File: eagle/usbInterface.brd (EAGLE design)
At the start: 40 x 20 mm, 22 parts

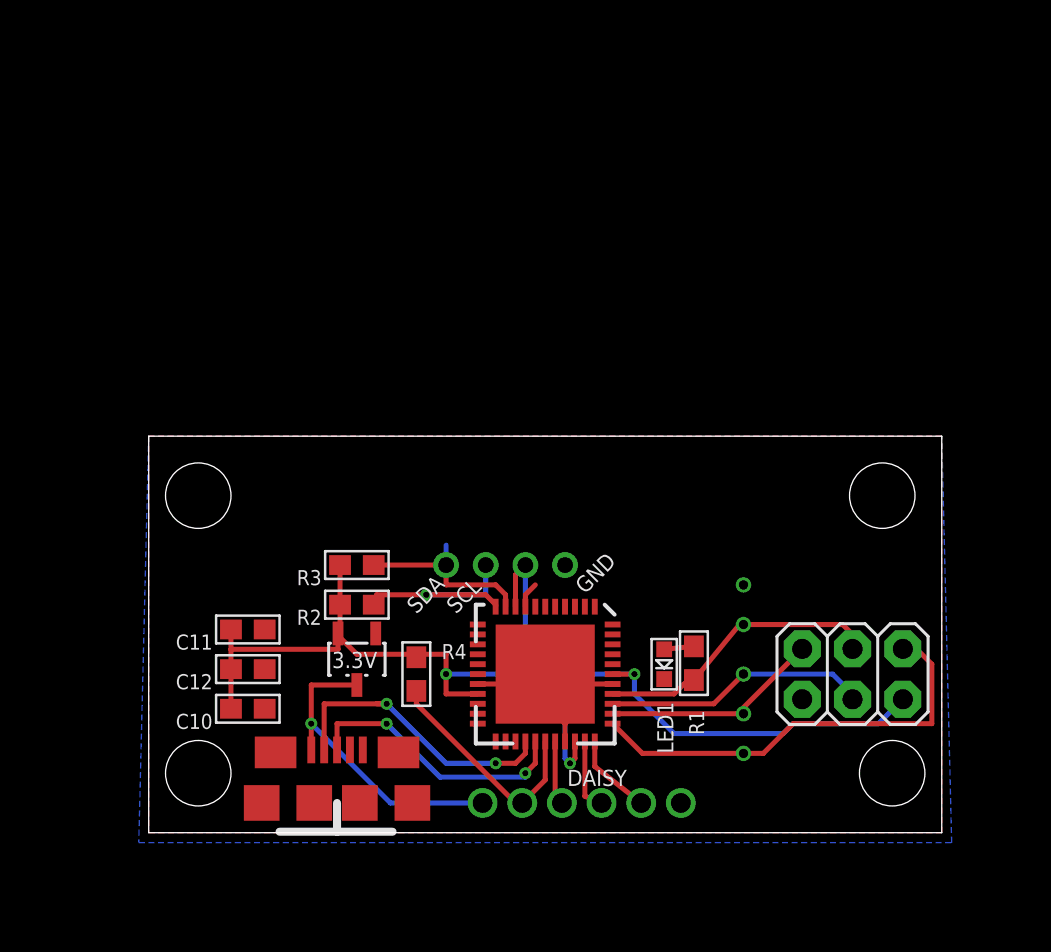
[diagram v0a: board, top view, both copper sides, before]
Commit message: large amount of work on 1x4 ewod array
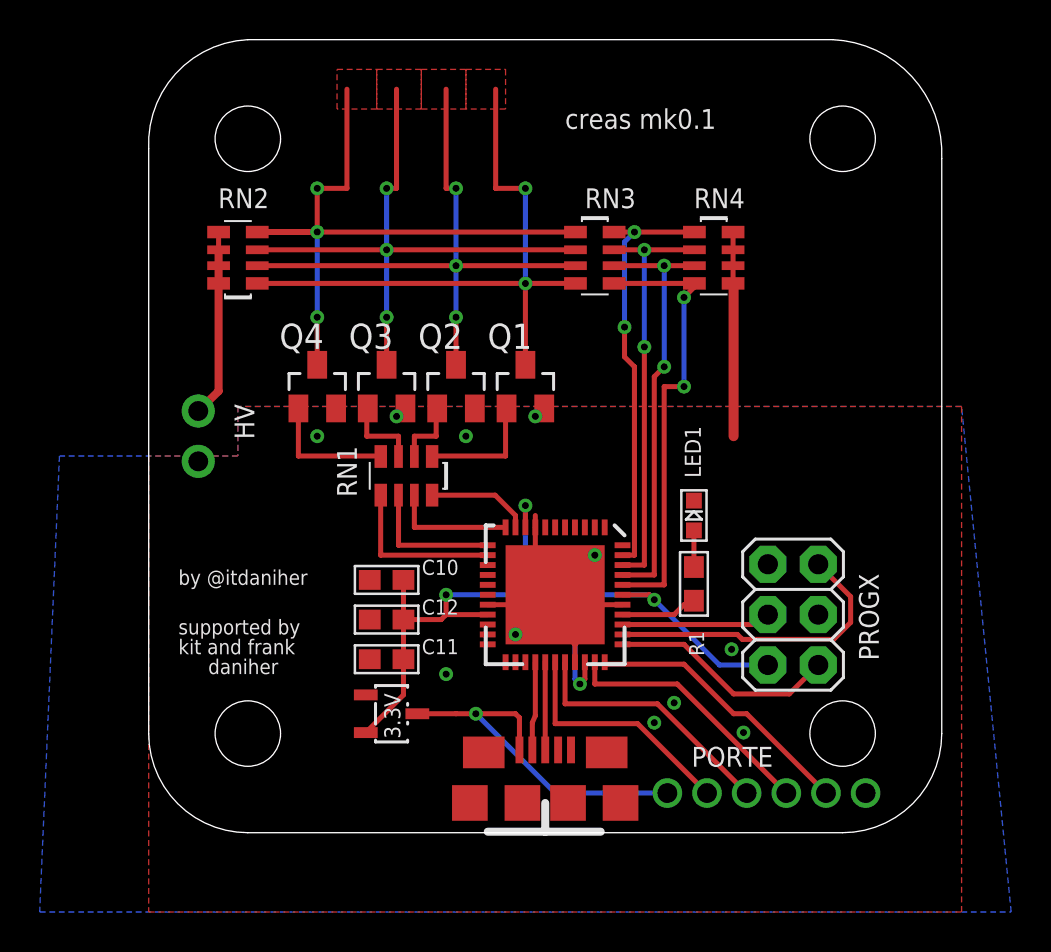
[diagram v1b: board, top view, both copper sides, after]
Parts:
- removed DAISY: (no value), nonolith:1X06_ROUND_2MM
- removed JP1, JP2, SCL, SDA: (no value), nonolith:1X01_2MM
- removed R2, R3: 4.7K, nonolith:0603
- removed R4: 4.7k, nonolith:0603
- added HV: (no value), nonolith:1X02_ROUND
- added PORTE: (no value), nonolith:1X06_ROUND_2MM
- added Q1, Q2, Q3, Q4: (no value), dp_devices:SOT23
- added RN1, RN2, RN3, RN4: (no value), nonolith:RN8P-4R-CRA06S
- moved U$3 18.2 mm to (-15.0, 35.0)
- moved U$4 18.1 mm to (15.0, 35.0)
- moved CN1 10.5 mm to (0.00, 1.50)
- moved C10 9.55 mm to (-8.00, 12.8), turned to 0 degrees
- moved LED1 7.65 mm to (7.50, 16.0), turned to 0 degrees
- moved C12 7.43 mm to (-8.00, 10.8), turned to 0 degrees
- moved C11 7.16 mm to (-8.00, 8.75), turned to 0 degrees
- moved PROGX 4.24 mm to (12.5, 11.0), turned to 90 degrees
- moved U$5 4.03 mm to (2.40, 10.1)
- moved XM1 4.03 mm to (0.50, 12.0)
- moved R1 4.00 mm to (7.50, 12.6)
- moved 3.3V 3.26 mm to (-7.75, 6.00), turned to 90 degrees
- moved U$1 3.20 mm to (-15.0, 5.00)
- moved U$2 3.20 mm to (15.0, 5.00)
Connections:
- removed net SCL: R2.1, SCL.1, XM1.11
- removed net SDA: R3.1, SDA.1, XM1.10
- new net ADCA: RN3.5, RN4.4, XM1.40
- new net ADCB: RN3.6, RN4.3, XM1.41
- new net ADCC: RN3.7, RN4.2, XM1.42
- new net ADCD: RN3.8, RN4.1, XM1.43
- new net CELLA: Q1.3, RN2.1, RN3.4
- new net CELLB: Q2.3, RN2.2, RN3.3
- new net CELLC: Q3.3, RN2.3, RN3.2
- new net CELLD: Q4.3, RN2.4, RN3.1
- new net GATEA: Q1.1, RN1.1
- new net GATEB: Q2.1, RN1.2
- new net GATEC: Q3.1, RN1.3
- new net GATED: Q4.1, RN1.4
- new net HV: HV.1, RN2.5, RN2.6, RN2.7, RN2.8
- new net OC0A: RN1.8, XM1.10
- new net OC0B: RN1.7, XM1.11
- new net OC0C: RN1.6, XM1.12
- new net OC0D: RN1.5, XM1.13
- net 3.3V: no longer JP2.1, R2.2, R3.2, R4.2
- net 5V: now also PORTE.1; no longer DAISY.6
- net GND: now also HV.2, PORTE.6, Q1.2, Q2.2, Q3.2, Q4.2, RN4.5, RN4.6, RN4.7, RN4.8; no longer DAISY.1, JP1.1
- net PE0: now also PORTE.2; no longer DAISY.5, R4.1
- net PE1: now also PORTE.3; no longer DAISY.4
- net PE2: now also PORTE.4; no longer DAISY.3
- net PE3: now also PORTE.5; no longer DAISY.2
- net PR1: no longer PROGX.3
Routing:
- net CELLD: track 0.00 -> 34.5 mm, vias 0 -> 3
- net CELLA: track 0.00 -> 31.5 mm, vias 0 -> 2
- net CELLC: track 0.00 -> 30.4 mm, vias 0 -> 3
- net CELLB: track 0.00 -> 30.4 mm, vias 0 -> 3
- net ADCA: track 0.00 -> 22.7 mm, vias 0 -> 2
- net ADCB: track 0.00 -> 21.5 mm, vias 0 -> 2
- net ADCD: track 0.00 -> 21.4 mm, vias 0 -> 2
- net ADCC: track 0.00 -> 21.0 mm, vias 0 -> 2
- net 3.3V: track 63.7 -> 44.6 mm, vias 3 -> 4
- net GND: track 11.2 -> 27.2 mm, vias 1 -> 11
- net SCL: track 11.5 -> 0.00 mm, vias 1 -> 0
- net HV: track 0.00 -> 11.2 mm
- net PR1: track 14.6 -> 3.85 mm, vias 1 -> 0
- net PDI-DATA: track 22.1 -> 11.5 mm, vias 1 -> 0
- net USB-: track 15.0 -> 4.46 mm, vias 2 -> 0
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- added copper zone on layer 1, net CELLA
- added copper zone on layer 1, net CELLB
- added copper zone on layer 1, net CELLC
- added copper zone on layer 1, net CELLD
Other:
- board size 40 x 20 mm -> 40 x 40 mm
- board text added: "by @itdaniher"
- board text added: "creas mk0.1"
- board text added: "daniher"
- board text added: "kit and frank"
- board text added: "supported by"
- board text removed: "GND"
- board text removed: "SCL"
- board text removed: "SDA"
